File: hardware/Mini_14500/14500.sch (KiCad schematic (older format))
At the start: 53 parts, among them J2 Battery, J3 GPIO, J4 USB_B_Micro, J5 Power, J6 LEDs, J7 GPIO, Q1 BSS806N, Q2 BSS806N, Q3 BSS806N, Q4 BSS806N, SW1 Mode, SW2 Power, U1 STM32L072KZTx, U2 AP2210N-3.3TRG1, U3 BQ21040, U4 ESD7002WTT1G, Y1 32.768kHz

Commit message: Add "mini" version
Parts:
- removed C10, C8: 7pF, Capacitor_SMD:C_0603_1608Metric, symbol Device:C_Small
- removed R14: 10k, Resistor_SMD:R_0603_1608Metric, symbol Device:R_Small
- removed U1: STM32L072KZTx, Package_QFP:LQFP-32_7x7mm_P0.8mm, symbol MCU_ST_STM32L0:STM32L072KZTx
- removed U3: BQ21040, Package_TO_SOT_SMD:SOT-23-6, symbol Jeremy:BQ21040
- removed Y1: 32.768kHz, Crystal:Crystal_SMD_3215-2Pin_3.2x1.5mm, symbol Device:Crystal_Small
- added U1: STM32L072KZUx, Package_DFN_QFN:QFN-32-1EP_5x5mm_P0.5mm_EP3.45x3.45mm, symbol MCU_ST_STM32L0:STM32L072KZUx
- added U3: MCP73831T-2ACI_OT, digikey-footprints:SOT-753, symbol dk_PMIC-Battery-Chargers:MCP73831T-2ACI_OT
- C11: value 1uf -> 4.7uF
- C9: value 1uF -> 4.7uF
- J2: footprint BatteryClips:Keystone54_18650_PTC -> BatteryClips:MDP_BK-82_14500
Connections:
- wire segments 204 -> 189
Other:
- note removed: "Optional RTC Source"
- moved on the sheet: C11, C9, D6, R11, R6

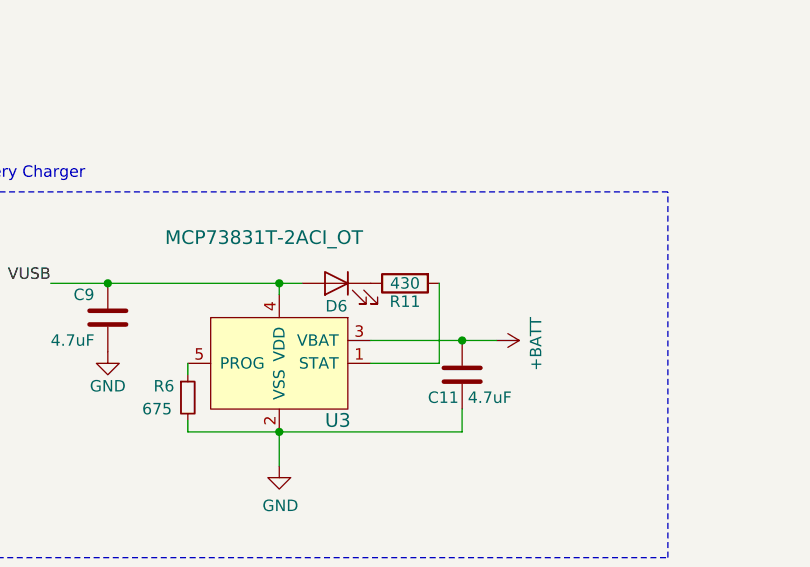
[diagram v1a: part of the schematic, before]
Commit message: Adjust space around battery terminals.
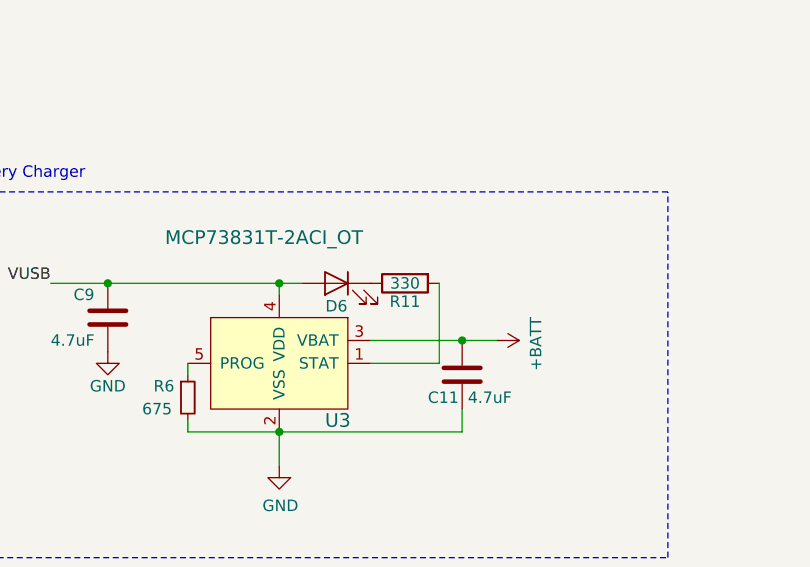
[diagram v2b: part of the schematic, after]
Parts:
- R11: value 430 -> 330
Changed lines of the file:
@@
 AR Path="/5DBBDA3F" Ref="R11"  Part="1"
 F 0 "R11" V 9530 5000 50  0000 C CNN
-F 1 "430" V 9450 5000 50  0000 C CNN
+F 1 "330" V 9450 5000 50  0000 C CNN
 F 2 "Resistor_SMD:R_0603_1608Metric" V 9380 5000 50  0001 C CNN
 F 3 "" H 9450 5000 50  0001 C CNN
